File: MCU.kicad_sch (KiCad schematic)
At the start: 15 parts, among them U5 STM32F405RGTx, Y1 LFXTAL055207Bulk

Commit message: Finished system overview
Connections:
- net USB_-DATA: now reaches U5.44 (PA11)
- net USB_+DATA: now reaches U5.45 (PA12)
- net FLASH_CS: no longer names the net of U5.33 (PB12)
- net PINIO1: no longer names the net of U5.35 (PB14)
- net SPI2_SCK: no longer names the net of U5.34 (PB13)
- net SPI2_SDI: no longer names the net of U5.10 (PC2)
- net SPI2_SDO: no longer names the net of U5.11 (PC3)
- net SPI3_SCK: no longer names the net of U5.55 (PB3)
- net SPI3_SDI: no longer names the net of U5.56 (PB4)
- net SPI3_SDO: no longer names the net of U5.57 (PB5)
- net UART1_TX: no longer names the net of U5.42 (PA9)
- net UART2_TX: no longer names the net of U5.16 (PA2)
- net UART3_RX: no longer names the net of U5.52 (PC11)
- net UART3_TX: no longer names the net of U5.51 (PC10)
- net UART6_RX: no longer names the net of U5.38 (PC7)
- net UART6_TX: no longer names the net of U5.37 (PC6)
- no-connect marks 3 -> 28

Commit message: Layout half-way done.
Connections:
- net AGND: no longer C10.2
- net DGND: now also C10.2
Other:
- note added: "Bulk Decoupling"
- moved on the sheet: C10, C6, C7

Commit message: Initial Wiring Complete
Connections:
- net I2C1_SCL renamed MCU_I2C1_SCL
- net I2C1_SDA renamed MCU_I2C1_SDA
- net SPI1_SCK renamed MCU_SPI1_SCK
- net SPI1_SDI renamed MCU_SPI1_SDI
- net SPI1_SDO renamed MCU_SPI1_SDO
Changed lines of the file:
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@@
 		(at 130.81 107.95)
 	)
-	(bus_entry
-		(at 95.25 113.03)
-		(size 2.54 2.54)
-		(stroke
-			(width 0)
-			(type default)
-		)
-	)
-	(bus_entry
-		(at 95.25 62.23)
-		(size 2.54 2.54)
-		(stroke
-			(width 0)
-			(type default)
-		)
-	)
-	(bus_entry
-		(at 95.25 115.57)
-		(size 2.54 2.54)
-		(stroke
-			(width 0)
-			(type default)
-		)
-	)
-	(bus_entry
-		(at 95.25 67.31)
-		(size 2.54 2.54)
-		(stroke
-			(width 0)
-			(type default)
-		)
-	)
-	(bus_entry
-		(at 95.25 64.77)
-		(size 2.54 2.54)
-		(stroke
-			(width 0)
-			(type default)
-		)
-	)
 	(wire
 		(pts
@@
 		)
 	)
-	(bus
-		(pts
-			(xy 95.25 62.23) (xy 88.9 62.23)
-		)
-		(stroke
-			(width 0)
-			(type default)
-		)
-	)
 	(wire
 		(pts
@@
 		)
 	)
-	(bus
-		(pts
-			(xy 95.25 67.31) (xy 95.25 69.85)
-		)
-		(stroke
-			(width 0)
-			(type default)
-		)
-	)
 	(wire
 		(pts
@@
 		)
 	)
-	(bus
-		(pts
-			(xy 95.25 62.23) (xy 95.25 64.77)
-		)
-		(stroke
-			(width 0)
-			(type default)
-		)
-	)
 	(wire
 		(pts
@@
 		)
 	)
-	(bus
-		(pts
-			(xy 95.25 64.77) (xy 95.25 67.31)
-		)
-		(stroke
-			(width 0)
-			(type default)
-		)
-	)
 	(wire
 		(pts
@@
 	(wire
 		(pts
-			(xy 97.79 115.57) (xy 130.81 115.57)
-		)
-		(stroke
-			(width 0)
-			(type default)
-		)
-	)
-	(wire
-		(pts
 			(xy 226.06 48.26) (xy 226.06 57.15)
 		)
@@
 	(wire
 		(pts
-			(xy 97.79 118.11) (xy 130.81 118.11)
-		)
-		(stroke
-			(width 0)
-			(type default)
-		)
-	)
-	(wire
-		(pts
 			(xy 177.8 29.21) (xy 177.8 30.48)
 		)
@@
 	(wire
 		(pts
-			(xy 97.79 64.77) (xy 130.81 64.77)
-		)
-		(stroke
-			(width 0)
-			(type default)
-		)
-	)
-	(bus
-		(pts
-			(xy 95.25 118.11) (xy 95.25 115.57)
-		)
-		(stroke
-			(width 0)
-			(type default)
-		)
-	)
-	(wire
-		(pts
 			(xy 257.81 49.53) (xy 257.81 48.26)
 		)
@@
 		)
 	)
-	(bus
-		(pts
-			(xy 95.25 115.57) (xy 95.25 113.03)
-		)
-		(stroke
-			(width 0)
-			(type default)
-		)
-	)
 	(wire
 		(pts
@@
 		)
 	)
-	(bus
-		(pts
-			(xy 88.9 113.03) (xy 95.25 113.03)
-		)
-		(stroke
-			(width 0)
-			(type default)
-		)
-	)
 	(wire
 		(pts
@@
 	(wire
 		(pts
-			(xy 97.79 67.31) (xy 130.81 67.31)
-		)
-		(stroke
-			(width 0)
-			(type default)
-		)
-	)
-	(wire
-		(pts
 			(xy 243.84 87.63) (xy 243.84 85.09)
 		)
@@
 			(width 0)
 			(type default)
-		)
-	)
-	(wire
-		(pts
-			(xy 97.79 69.85) (xy 130.81 69.85)
-		)
-		(stroke
-			(width 0)
-			(type default)
-		)
-	)
-	(label "I2C1_SDA"
-		(at 97.79 118.11 0)
-		(effects
-			(font
-				(size 1.27 1.27)
-			)
-			(justify left bottom)
-		)
-	)
-	(label "I2C1_SCL"
-		(at 97.79 115.57 0)
-		(effects
-			(font
-				(size 1.27 1.27)
-			)
-			(justify left bottom)
 		)
 	)
@@
 		)
 	)
-	(label "SPI1_SDO"
-		(at 97.79 69.85 0)
-		(effects
-			(font
-				(size 1.27 1.27)
-			)
-			(justify left bottom)
-		)
-	)
-	(label "SPI1_SDI"
-		(at 97.79 67.31 0)
-		(effects
-			(font
-				(size 1.27 1.27)
-			)
-			(justify left bottom)
-		)
-	)
-	(label "SPI1_SCK"
-		(at 97.79 64.77 0)
-		(effects
-			(font
-				(size 1.27 1.27)
-			)
-			(justify left bottom)
-		)
-	)
 	(label "CLK_OUT"
 		(at 245.11 85.09 0)
@@
 		)
 	)
-	(hierarchical_label "{I2C1}"
-		(shape bidirectional)
-		(at 88.9 113.03 180)
-		(effects
-			(font
-				(size 1.27 1.27)
-			)
-			(justify right)
-		)
-	)
-	(hierarchical_label "{SPI1}"
-		(shape bidirectional)
-		(at 88.9 62.23 180)
+	(hierarchical_label "MCU_I2C1_SCL"
+		(shape input)
+		(at 130.81 115.57 180)
 		(effects
 			(font
@@
 		)
 	)
+	(hierarchical_label "MCU_SPI1_SCK"
+		(shape input)
+		(at 130.81 64.77 180)
+		(effects
+			(font
+				(size 1.27 1.27)
+			)
+			(justify right)
+		)
+	)
 	(hierarchical_label "IMU_EXTI"
 		(shape input)
@@
 		)
 	)
+	(hierarchical_label "MCU_SPI1_SDO"
+		(shape input)
+		(at 130.81 69.85 180)
+		(effects
+			(font
+				(size 1.27 1.27)
+			)
+			(justify right)
+		)
+	)
+	(hierarchical_label "MCU_SPI1_SDI"
+		(shape input)
+		(at 130.81 67.31 180)
+		(effects
+			(font
+				(size 1.27 1.27)
+			)
+			(justify right)
+		)
+	)
 	(hierarchical_label "USB_-DATA"
 		(shape input)
@@
 		(effects
 			(font
+				(size 1.27 1.27)
+			)
+			(justify right)
+		)
+	)
+	(hierarchical_label "MCU_I2C1_SDA"
+		(shape input)
+		(at 130.81 118.11 180)
+		(effects
+			(font

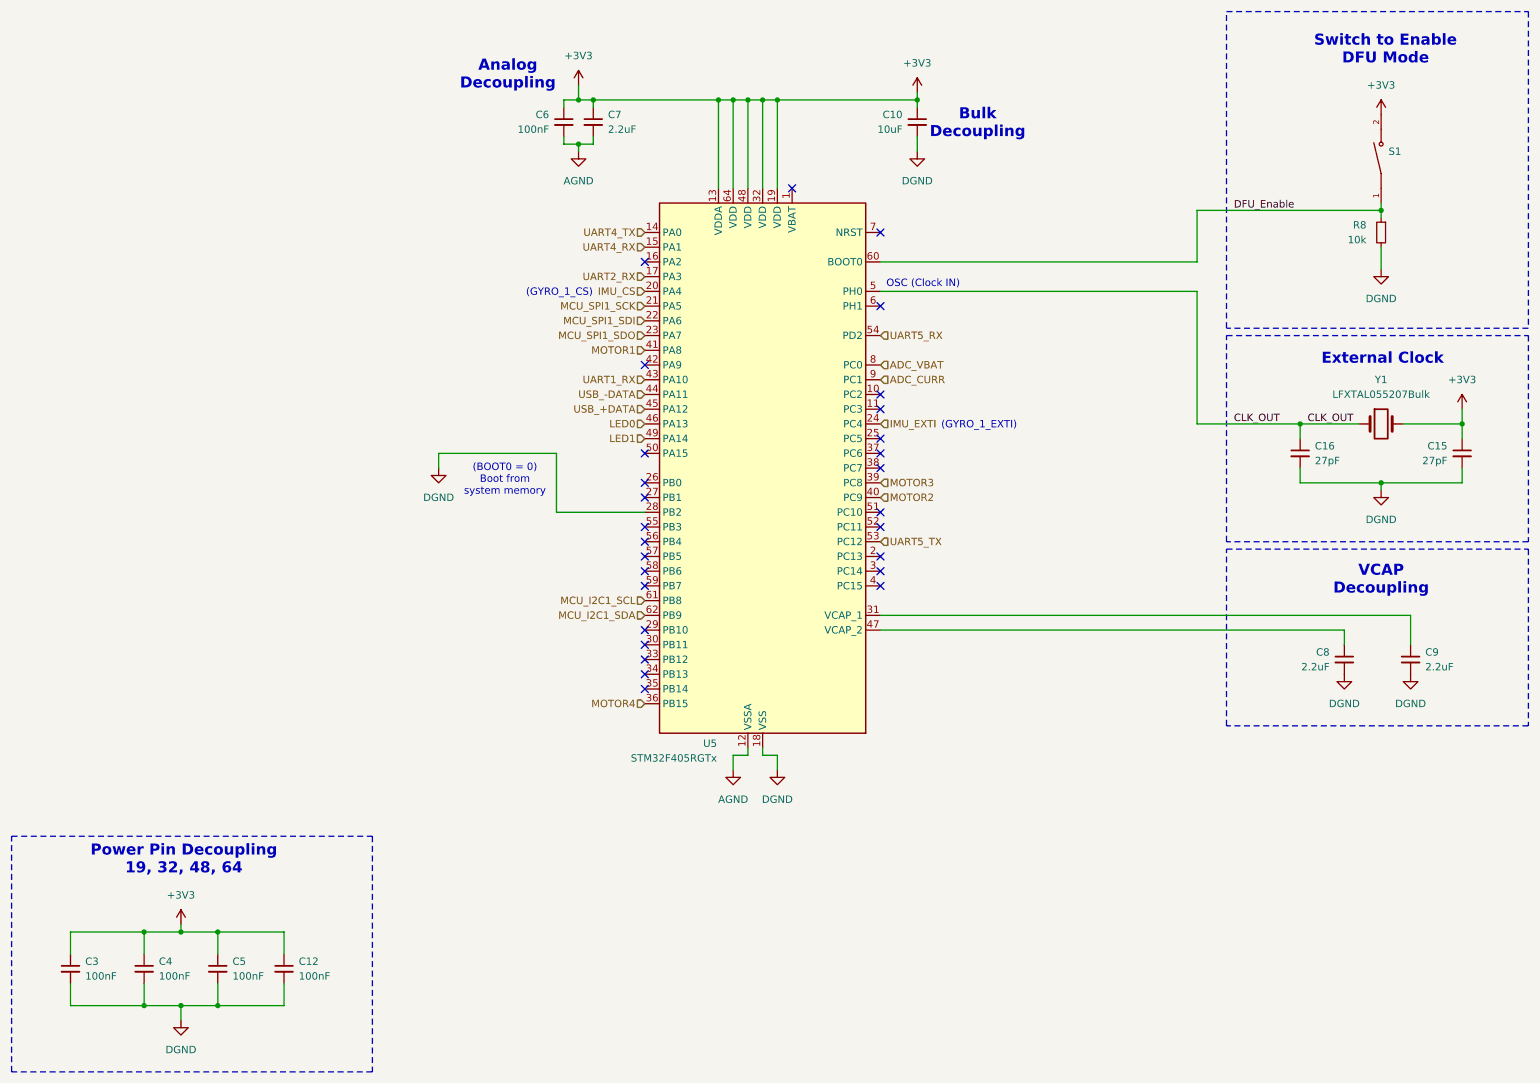
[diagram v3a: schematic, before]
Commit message: Added part-numbers and updated symbols
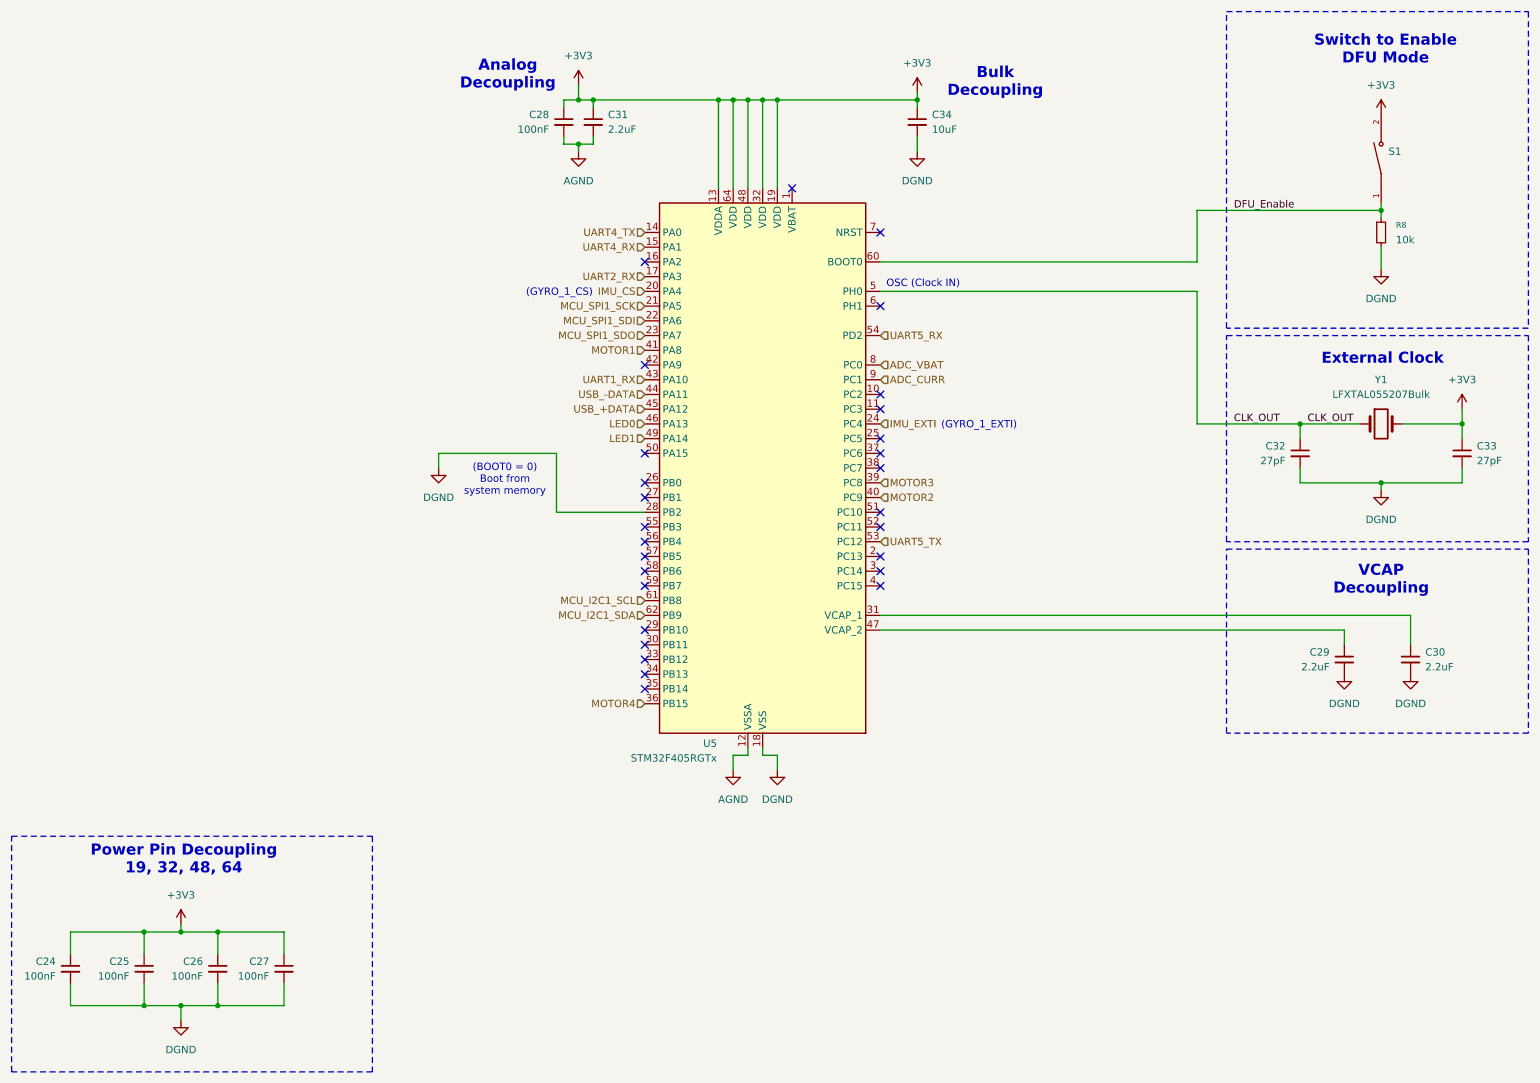
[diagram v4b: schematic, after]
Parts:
- removed C10: 10uF, Capacitor_SMD:C_0603_1608Metric_Pad1.08x0.95mm_HandSolder, symbol Device:C_Small
- removed C12, C3, C4, C5, C6: 100nF, Capacitor_SMD:C_0603_1608Metric_Pad1.08x0.95mm_HandSolder, symbol Device:C_Small
- removed C15, C16: 27pF, Capacitor_SMD:C_0603_1608Metric_Pad1.08x0.95mm_HandSolder, symbol Device:C_Small
- removed C7, C8, C9: 2.2uF, Capacitor_SMD:C_0603_1608Metric_Pad1.08x0.95mm_HandSolder, symbol Device:C_Small
- removed R8: 10k, Resistor_SMD:R_0603_1608Metric_Pad0.98x0.95mm_HandSolder, symbol Device:R_Small
- added C24, C25, C26, C27, C28: 100nF, Capacitor_SMD:C_0402_1005Metric, symbol KSE_Capacitors:C_Small
- added C29, C30, C31: 2.2uF, Capacitor_SMD:C_0402_1005Metric, symbol KSE_Capacitors:C_Small
- added C32, C33: 27pF, Capacitor_SMD:C_0603_1608Metric, symbol KSE_Capacitors:C_Small
- added C34: 10uF, Capacitor_SMD:C_0402_1005Metric, symbol KSE_Capacitors:C_Small
- added R8: 10k, Resistor_SMD:R_0402_1005Metric, symbol KSE_Resistors:R_Small
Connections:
- net +3V3: now also C24.1, C25.1, C26.1, C27.1, C28.1, C31.1, C33.1, C34.1
- net AGND: now also C28.2, C31.2
- net CLK_OUT: now also C32.1
- net DFU_Enable: now also R8.1
- net DGND: now also C24.2, C25.2, C26.2, C27.2, C29.2, C30.2, C32.2, C33.2, C34.2, R8.2
- net at U5.47 (VCAP_2): now also C29.1
- net at U5.31 (VCAP_1): now also C30.1

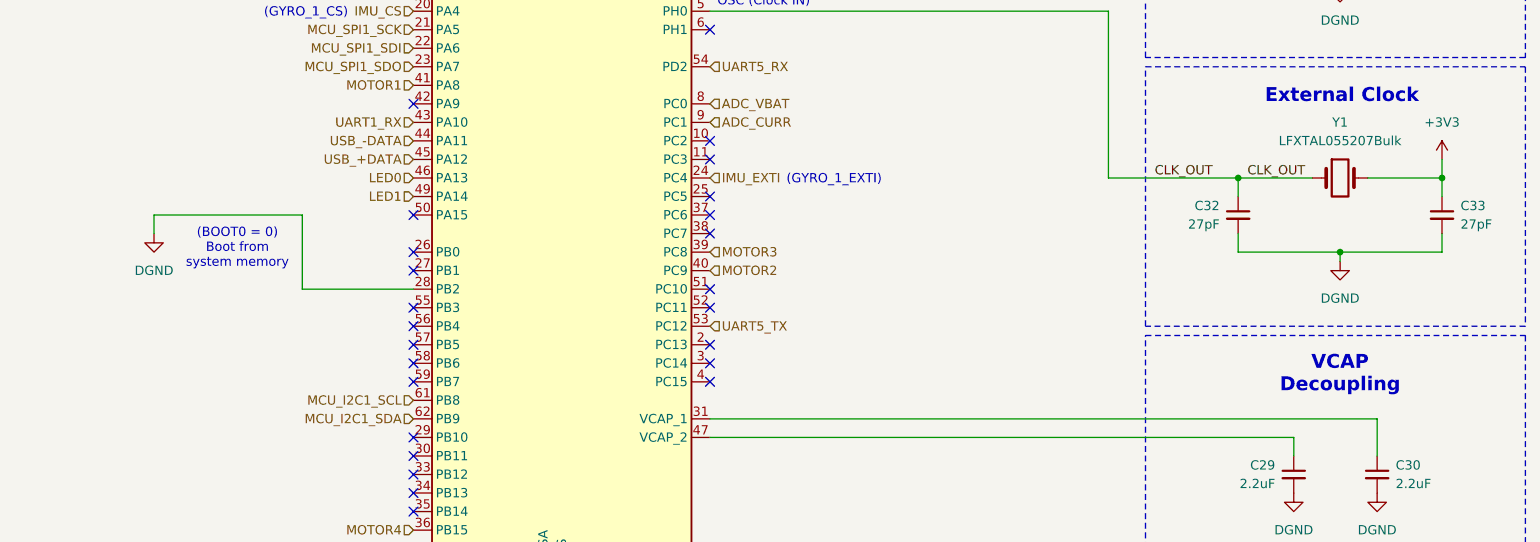
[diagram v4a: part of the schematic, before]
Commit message: Added part-numbers and updated symbols
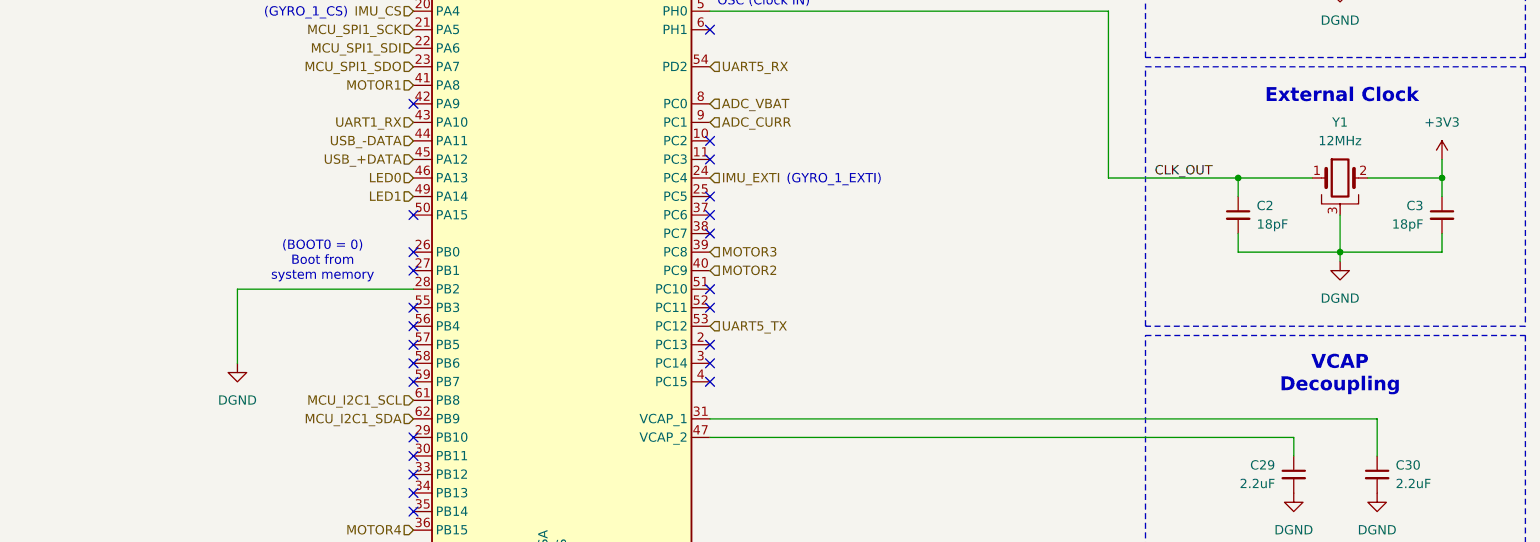
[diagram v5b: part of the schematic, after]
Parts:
- removed C32, C33: 27pF, Capacitor_SMD:C_0603_1608Metric, symbol KSE_Capacitors:C_Small
- removed Y1: LFXTAL055207Bulk, KSE_passive:Crystal_HC49-4H_Vertical, symbol KSE_passive:crystal_8MHz_THT_LFXTAL055207Bulk
- added C2, C3: 18pF, Capacitor_SMD:C_0603_1608Metric, symbol KSE_Capacitors:C_Small
- added Y1: 12MHz, Crystal:Crystal_SMD_Abracon_ABM8AIG-4Pin_3.2x2.5mm, symbol KSE_passive:Crystal_4-Pin
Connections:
- net +3V3: now also C3.1, Y1.2
- net CLK_OUT: now also C2.1, Y1.1
- net DGND: now also C2.2, C3.2, Y1.3 (GND), Y1.4 (GND)
